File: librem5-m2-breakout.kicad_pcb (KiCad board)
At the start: 4 copper layers, 30 x 22 mm, 16 parts, among them J101 M.2_Key_E, J102 Conn_01x02, J103 Conn_02x03_Counter_Clockwise, J104 Conn_02x03_Counter_Clockwise, J105 Conn_01x01, J106 Conn_01x03, J107 Conn_01x02, J108 USB_B_Micro, J109 Micro_SD, U101 SN74LV1T34DBV

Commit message: Add 2-layer board that's only for UART4
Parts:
- removed J102: Conn_01x02, Connector_PinHeader_2.54mm:PinHeader_1x02_P2.54mm_Vertical
- removed J103, J104: Conn_02x03_Counter_Clockwise, Connector_PinHeader_1.27mm:PinHeader_2x03_P1.27mm_Vertical_SMD
- removed J107: Conn_01x02, Connector_PinHeader_1.27mm:PinHeader_1x02_P1.27mm_Vertical_SMD_Pin1Right
- removed J108: USB_B_Micro, Connector_USB:USB_Micro-B_Wuerth_614105150721_Vertical
- removed J109: Micro_SD, librem5-m2-breakout:ALPS_SCHA4B0419
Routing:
- net /~SDIO_WAKE: track 48.8 -> 0.00 mm, vias 2 -> 0
- net /~SDIO_RST: track 46.0 -> 0.00 mm, vias 2 -> 0
- net /I2S_TXC: track 41.5 -> 0.00 mm, vias 3 -> 0
- net /WIFI_REG_ON: track 40.1 -> 0.00 mm, vias 1 -> 0
- net /BT_REG_ON: track 39.1 -> 0.00 mm, vias 1 -> 0
- net /I2S_TXFS: track 34.8 -> 0.00 mm, vias 1 -> 0
- net /BT_WAKE: track 33.1 -> 0.00 mm, vias 1 -> 0
- net /SDIO_DATA0: track 31.7 -> 0.00 mm
- net /I2S_TXD: track 31.4 -> 0.00 mm, vias 1 -> 0
- net /I2S_RXD: track 30.6 -> 0.00 mm, vias 1 -> 0
- net /SDIO_CMD: track 29.0 -> 0.00 mm, vias 2 -> 0
- net /SDIO_CLK: track 26.6 -> 0.00 mm, vias 2 -> 0
- net +3V3: track 27.4 -> 53.1 mm, vias 5 -> 3
- net /SDIO_DATA3: track 25.6 -> 0.00 mm
- net /UART_RTS: track 25.4 -> 0.00 mm, vias 1 -> 0
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- removed copper zone on In2.Cu, net +3V3
- removed copper zone on In1.Cu, net GND
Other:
- copper layers 4 -> 2
- board text removed: "3V3"
- board text removed: "CTS"
- board text removed: "RTS"
- board text removed: "RXD"
- board text removed: "TXC"
- board text removed: "TXD"
- board text removed: "TXFS"

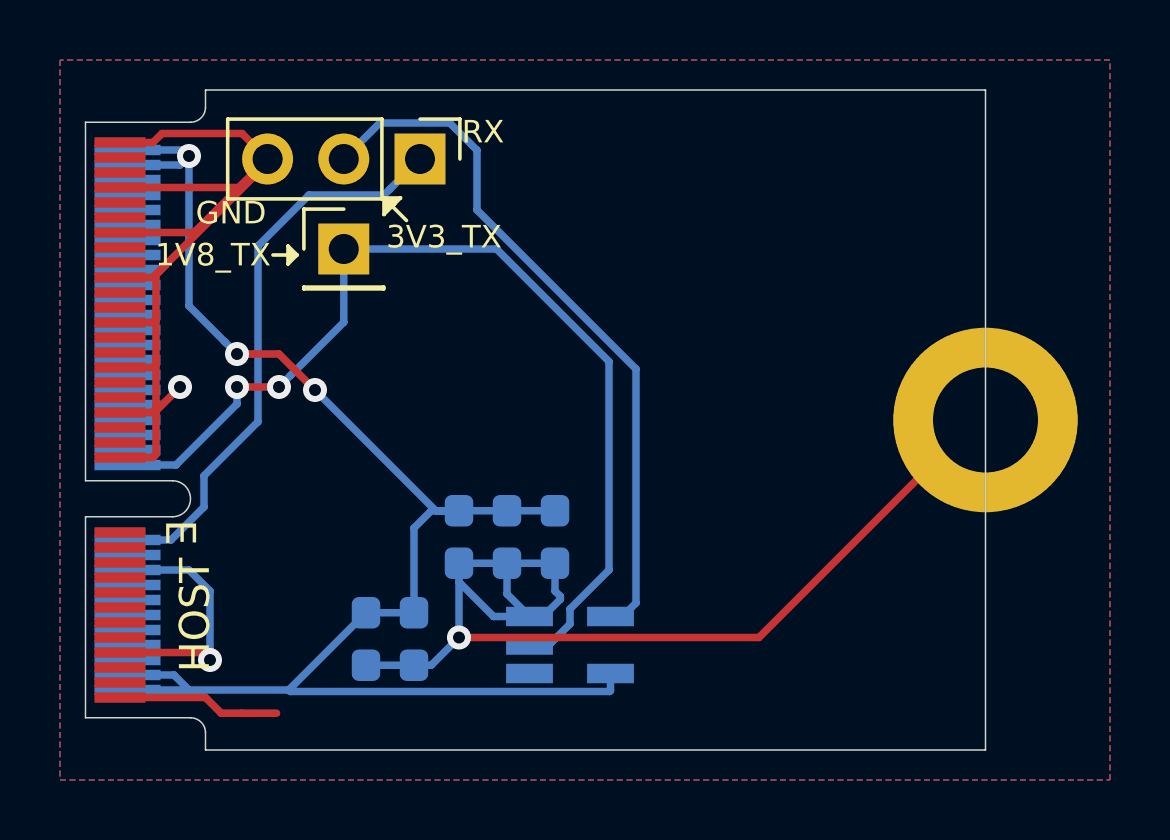
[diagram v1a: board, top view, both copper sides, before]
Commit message: Make it so that the back side of the M.2 mounting hole has a solid copper flood attached to it
Add some stitching vias, joining the top and bottom ground planes in a
few more spots.
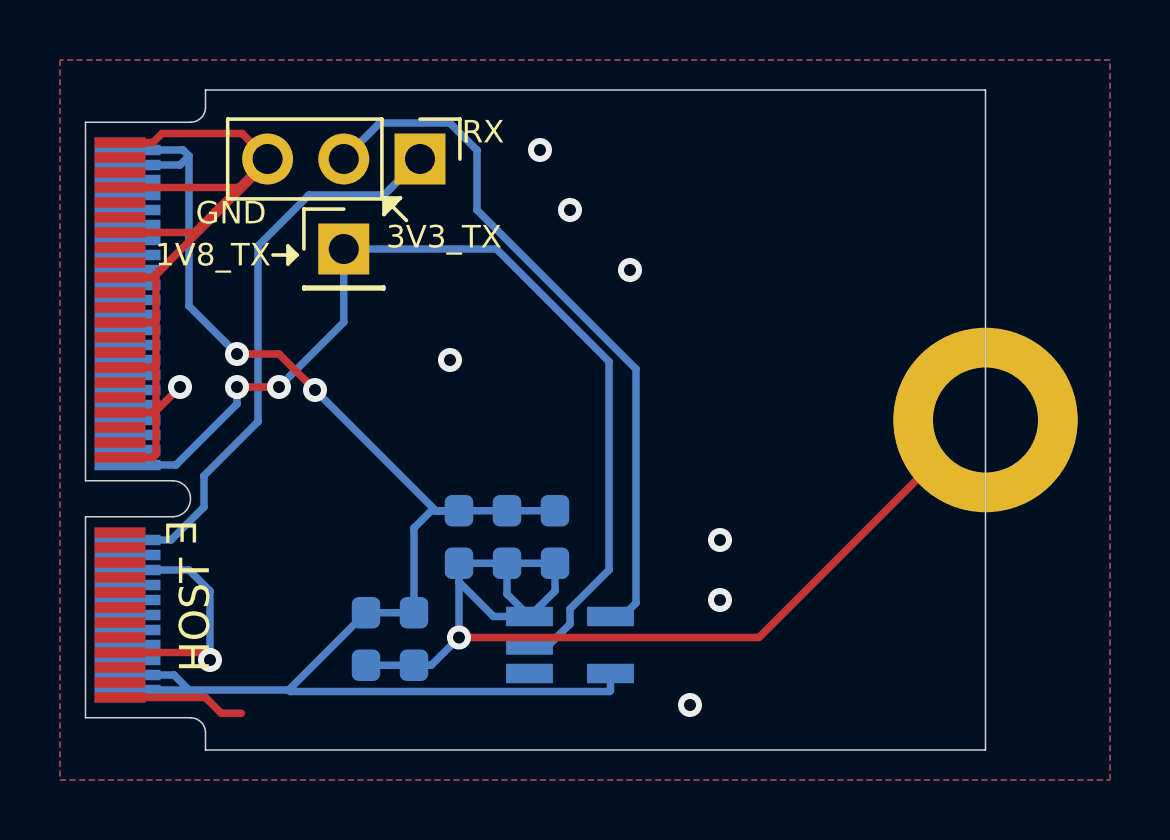
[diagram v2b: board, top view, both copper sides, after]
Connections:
- net /~SDIO_RST renamed /~{SDIO_RST}
- net /~SDIO_WAKE renamed /~{SDIO_WAKE}
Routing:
- net GND: track 87.4 -> 85.8 mm, vias 3 -> 10
- net +3V3: vias 3 -> 2
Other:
- net class Default removed
- net class USB removed
